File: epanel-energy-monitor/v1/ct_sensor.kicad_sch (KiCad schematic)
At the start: 8 parts

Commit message: add small terminal footprint
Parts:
- J?: footprint (none) -> mylife-footprints:RS PRO Terminal Small x2
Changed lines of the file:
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@@
       (effects (font (size 1.27 1.27)) (justify left))
     )
-    (property "Footprint" "" (id 2) (at 209.55 76.2 0)
+    (property "Footprint" "mylife-footprints:RS PRO Terminal Small x2" (id 2) (at 209.55 76.2 0)
       (effects (font (size 1.27 1.27)) hide)
     )
-    (property "Datasheet" "~" (id 3) (at 209.55 76.2 0)
+    (property "Datasheet" "https://docs.rs-online.com/90f4/0900766b8157c7e9.pdf" (id 3) (at 209.55 76.2 0)
       (effects (font (size 1.27 1.27)) hide)
     )

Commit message: rotary switch
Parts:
- removed J?: Conn_02x05, Connector_PinHeader_2.54mm:PinHeader_2x05_P2.54mm_Vertical, symbol Connector_Generic:Conn_02x05_Odd_Even
- added S15: SS-10-15SPE, mylife-footprints:RS PRO SS-10-15SPE, symbol mylife-symbols:SS-10-15SPE
- gave numbers to parts that had none: 7
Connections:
- net ZERO: now also S15.2 (Common), S15.7 (Common)
- net at R96.2: now also S15.3 (pos_2)
- net at R98.2: now also S15.5 (pos_4)
- net at R99.2: now also S15.6 (pos_5)
- net at R95.2: now also S15.1 (pos_1)
- net at R97.2: now also S15.4 (pos_3)

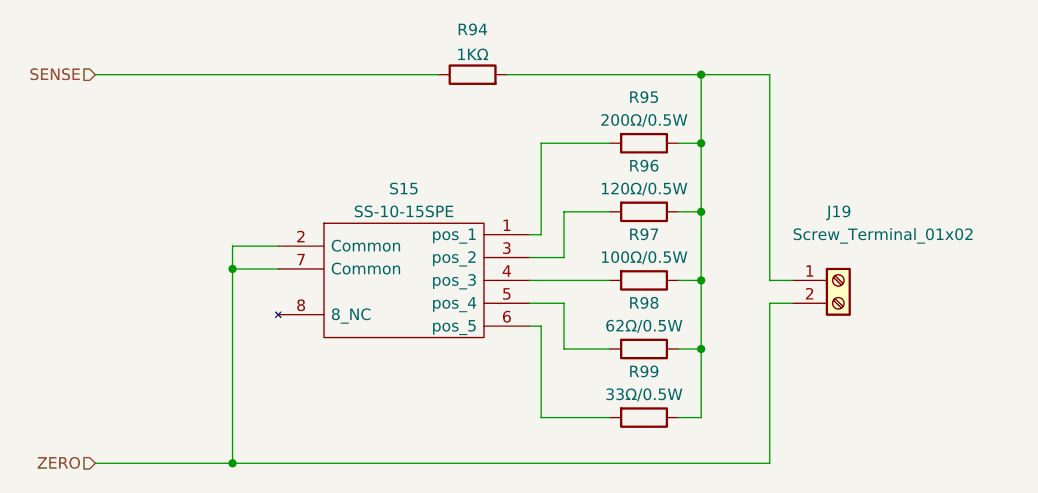
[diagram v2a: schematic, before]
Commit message: schematic remove esp
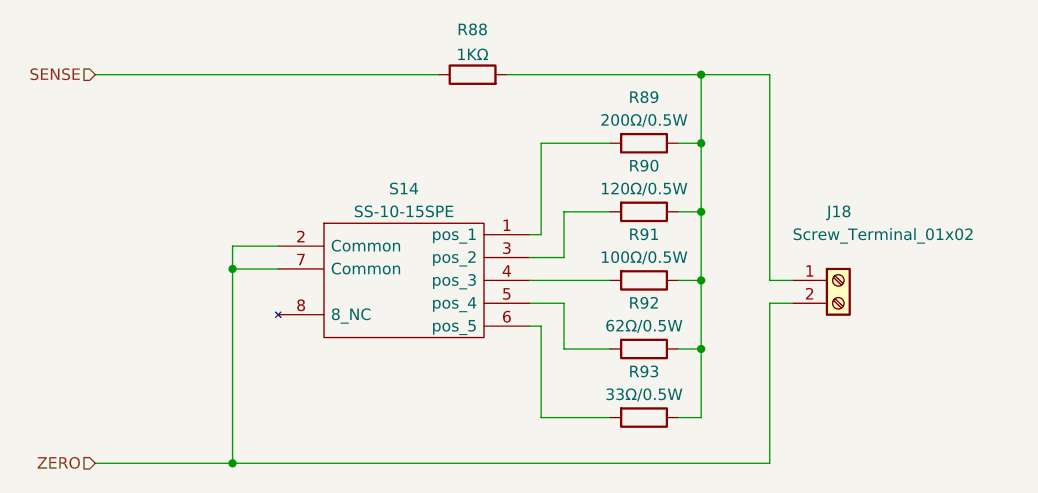
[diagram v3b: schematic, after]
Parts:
- renumbered J19 to J18, R94 to R88, R95 to R89, R96 to R90, R97 to R91, R98 to R92, R99 to R93, S15 to S14
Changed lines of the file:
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@@
   (symbol (lib_id "Device:R") (at 187.96 68.58 270)
     (in_bom yes) (on_board yes)
-    (property "Reference" "R96" (id 0) (at 187.96 63.5 90))
+    (property "Reference" "R90" (id 0) (at 187.96 63.5 90))
     (property "Value" "120Ω/0.5W" (id 1) (at 187.96 66.04 90))
     (property "Footprint" "Resistor_SMD:R_0805_2012Metric" (id 2) (at 187.96 66.802 90)
@@
   (symbol (lib_id "Device:R") (at 187.96 83.82 270)
     (in_bom yes) (on_board yes)
-    (property "Reference" "R98" (id 0) (at 187.96 78.74 90))
+    (property "Reference" "R92" (id 0) (at 187.96 78.74 90))
     (property "Value" "62Ω/0.5W" (id 1) (at 187.96 81.28 90))
     (property "Footprint" "Resistor_SMD:R_0805_2012Metric" (id 2) (at 187.96 82.042 90)
@@
   (symbol (lib_id "Device:R") (at 168.91 53.34 90)
     (in_bom yes) (on_board yes) (fields_autoplaced)
-    (property "Reference" "R94" (id 0) (at 168.91 48.3575 90))
+    (property "Reference" "R88" (id 0) (at 168.91 48.3575 90))
     (property "Value" "1KΩ" (id 1) (at 168.91 51.1326 90))
     (property "Footprint" "Resistor_SMD:R_0603_1608Metric" (id 2) (at 168.91 55.118 90)
@@
   (symbol (lib_id "Connector:Screw_Terminal_01x02") (at 209.55 76.2 0)
     (in_bom yes) (on_board yes)
-    (property "Reference" "J19" (id 0) (at 208.28 68.58 0)
+    (property "Reference" "J18" (id 0) (at 208.28 68.58 0)
       (effects (font (size 1.27 1.27)) (justify left))
     )
@@
   (symbol (lib_id "Device:R") (at 187.96 60.96 270)
     (in_bom yes) (on_board yes)
-    (property "Reference" "R95" (id 0) (at 187.96 55.88 90))
+    (property "Reference" "R89" (id 0) (at 187.96 55.88 90))
     (property "Value" "200Ω/0.5W" (id 1) (at 187.96 58.42 90))
     (property "Footprint" "Resistor_SMD:R_0805_2012Metric" (id 2) (at 187.96 59.182 90)
@@
   (symbol (lib_id "mylife-symbols:SS-10-15SPE") (at 161.29 76.2 0)
     (in_bom yes) (on_board yes)
-    (property "Reference" "S15" (id 0) (at 161.29 66.04 0))
+    (property "Reference" "S14" (id 0) (at 161.29 66.04 0))
     (property "Value" "SS-10-15SPE" (id 1) (at 161.29 68.58 0))
     (property "Footprint" "mylife-footprints:RS PRO SS-10-15SPE" (id 2) (at 185.42 73.66 0)
@@
   (symbol (lib_id "Device:R") (at 187.96 91.44 270)
     (in_bom yes) (on_board yes)
-    (property "Reference" "R99" (id 0) (at 187.96 86.36 90))
+    (property "Reference" "R93" (id 0) (at 187.96 86.36 90))
     (property "Value" "33Ω/0.5W" (id 1) (at 187.96 88.9 90))
     (property "Footprint" "Resistor_SMD:R_0805_2012Metric" (id 2) (at 187.96 89.662 90)
@@
   (symbol (lib_id "Device:R") (at 187.96 76.2 270)
     (in_bom yes) (on_board yes)
-    (property "Reference" "R97" (id 0) (at 187.96 71.12 90))
+    (property "Reference" "R91" (id 0) (at 187.96 71.12 90))
     (property "Value" "100Ω/0.5W" (id 1) (at 187.96 73.66 90))
     (property "Footprint" "Resistor_SMD:R_0805_2012Metric" (id 2) (at 187.96 74.422 90)

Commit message: enery monitor schematic
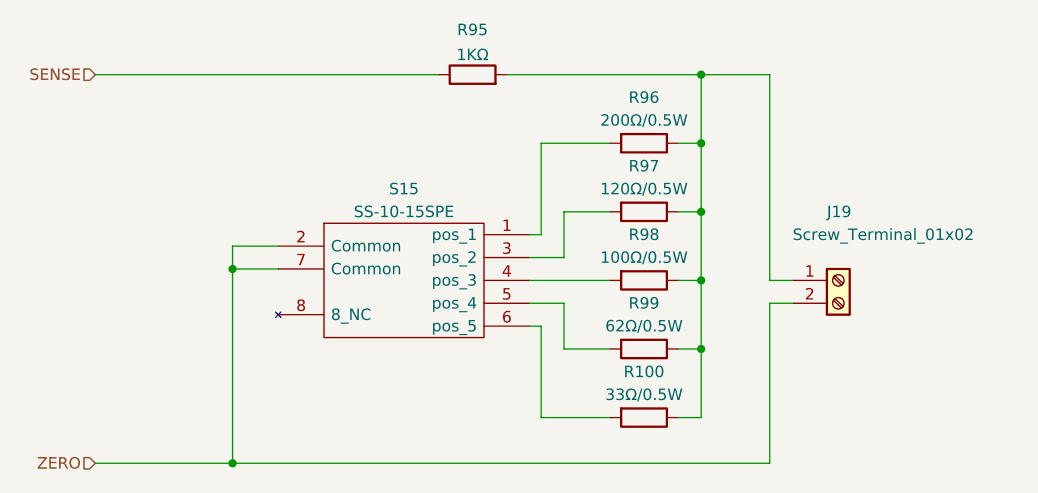
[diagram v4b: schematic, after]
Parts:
- renumbered J18 to J19, R93 to R100, R88 to R95, R89 to R96, R90 to R97, R91 to R98, R92 to R99, S14 to S15
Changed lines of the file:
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@@
   (symbol (lib_id "Device:R") (at 187.96 68.58 270)
     (in_bom yes) (on_board yes)
-    (property "Reference" "R90" (id 0) (at 187.96 63.5 90))
+    (property "Reference" "R97" (id 0) (at 187.96 63.5 90))
     (property "Value" "120Ω/0.5W" (id 1) (at 187.96 66.04 90))
     (property "Footprint" "Resistor_SMD:R_0805_2012Metric" (id 2) (at 187.96 66.802 90)
@@
   (symbol (lib_id "Device:R") (at 187.96 83.82 270)
     (in_bom yes) (on_board yes)
-    (property "Reference" "R92" (id 0) (at 187.96 78.74 90))
+    (property "Reference" "R99" (id 0) (at 187.96 78.74 90))
     (property "Value" "62Ω/0.5W" (id 1) (at 187.96 81.28 90))
     (property "Footprint" "Resistor_SMD:R_0805_2012Metric" (id 2) (at 187.96 82.042 90)
@@
   (symbol (lib_id "Device:R") (at 168.91 53.34 90)
     (in_bom yes) (on_board yes) (fields_autoplaced)
-    (property "Reference" "R88" (id 0) (at 168.91 48.3575 90))
+    (property "Reference" "R95" (id 0) (at 168.91 48.3575 90))
     (property "Value" "1KΩ" (id 1) (at 168.91 51.1326 90))
     (property "Footprint" "Resistor_SMD:R_0603_1608Metric" (id 2) (at 168.91 55.118 90)
@@
   (symbol (lib_id "Connector:Screw_Terminal_01x02") (at 209.55 76.2 0)
     (in_bom yes) (on_board yes)
-    (property "Reference" "J18" (id 0) (at 208.28 68.58 0)
+    (property "Reference" "J19" (id 0) (at 208.28 68.58 0)
       (effects (font (size 1.27 1.27)) (justify left))
     )
@@
   (symbol (lib_id "Device:R") (at 187.96 60.96 270)
     (in_bom yes) (on_board yes)
-    (property "Reference" "R89" (id 0) (at 187.96 55.88 90))
+    (property "Reference" "R96" (id 0) (at 187.96 55.88 90))
     (property "Value" "200Ω/0.5W" (id 1) (at 187.96 58.42 90))
     (property "Footprint" "Resistor_SMD:R_0805_2012Metric" (id 2) (at 187.96 59.182 90)
@@
   (symbol (lib_id "mylife-symbols:SS-10-15SPE") (at 161.29 76.2 0)
     (in_bom yes) (on_board yes)
-    (property "Reference" "S14" (id 0) (at 161.29 66.04 0))
+    (property "Reference" "S15" (id 0) (at 161.29 66.04 0))
     (property "Value" "SS-10-15SPE" (id 1) (at 161.29 68.58 0))
     (property "Footprint" "mylife-footprints:RS PRO SS-10-15SPE" (id 2) (at 185.42 73.66 0)
@@
   (symbol (lib_id "Device:R") (at 187.96 91.44 270)
     (in_bom yes) (on_board yes)
-    (property "Reference" "R93" (id 0) (at 187.96 86.36 90))
+    (property "Reference" "R100" (id 0) (at 187.96 86.36 90))
     (property "Value" "33Ω/0.5W" (id 1) (at 187.96 88.9 90))
     (property "Footprint" "Resistor_SMD:R_0805_2012Metric" (id 2) (at 187.96 89.662 90)
@@
   (symbol (lib_id "Device:R") (at 187.96 76.2 270)
     (in_bom yes) (on_board yes)
-    (property "Reference" "R91" (id 0) (at 187.96 71.12 90))
+    (property "Reference" "R98" (id 0) (at 187.96 71.12 90))
     (property "Value" "100Ω/0.5W" (id 1) (at 187.96 73.66 90))
     (property "Footprint" "Resistor_SMD:R_0805_2012Metric" (id 2) (at 187.96 74.422 90)

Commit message: wip energy pcb
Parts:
- renumbered J19 to J5, R95 to R11, R96 to R12, R97 to R13, R98 to R14, R99 to R15, R100 to R16, S15 to S1
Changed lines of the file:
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@@
   (symbol (lib_id "Device:R") (at 187.96 68.58 270)
     (in_bom yes) (on_board yes)
-    (property "Reference" "R97" (id 0) (at 187.96 63.5 90))
+    (property "Reference" "R13" (id 0) (at 187.96 63.5 90))
     (property "Value" "120Ω/0.5W" (id 1) (at 187.96 66.04 90))
     (property "Footprint" "Resistor_SMD:R_0805_2012Metric" (id 2) (at 187.96 66.802 90)
@@
   (symbol (lib_id "Device:R") (at 187.96 83.82 270)
     (in_bom yes) (on_board yes)
-    (property "Reference" "R99" (id 0) (at 187.96 78.74 90))
+    (property "Reference" "R15" (id 0) (at 187.96 78.74 90))
     (property "Value" "62Ω/0.5W" (id 1) (at 187.96 81.28 90))
     (property "Footprint" "Resistor_SMD:R_0805_2012Metric" (id 2) (at 187.96 82.042 90)
@@
   (symbol (lib_id "Device:R") (at 168.91 53.34 90)
     (in_bom yes) (on_board yes) (fields_autoplaced)
-    (property "Reference" "R95" (id 0) (at 168.91 48.3575 90))
+    (property "Reference" "R11" (id 0) (at 168.91 48.3575 90))
     (property "Value" "1KΩ" (id 1) (at 168.91 51.1326 90))
     (property "Footprint" "Resistor_SMD:R_0603_1608Metric" (id 2) (at 168.91 55.118 90)
@@
   (symbol (lib_id "Connector:Screw_Terminal_01x02") (at 209.55 76.2 0)
     (in_bom yes) (on_board yes)
-    (property "Reference" "J19" (id 0) (at 208.28 68.58 0)
+    (property "Reference" "J5" (id 0) (at 208.28 68.58 0)
       (effects (font (size 1.27 1.27)) (justify left))
     )
@@
   (symbol (lib_id "Device:R") (at 187.96 60.96 270)
     (in_bom yes) (on_board yes)
-    (property "Reference" "R96" (id 0) (at 187.96 55.88 90))
+    (property "Reference" "R12" (id 0) (at 187.96 55.88 90))
     (property "Value" "200Ω/0.5W" (id 1) (at 187.96 58.42 90))
     (property "Footprint" "Resistor_SMD:R_0805_2012Metric" (id 2) (at 187.96 59.182 90)
@@
   (symbol (lib_id "mylife-symbols:SS-10-15SPE") (at 161.29 76.2 0)
     (in_bom yes) (on_board yes)
-    (property "Reference" "S15" (id 0) (at 161.29 66.04 0))
+    (property "Reference" "S1" (id 0) (at 161.29 66.04 0))
     (property "Value" "SS-10-15SPE" (id 1) (at 161.29 68.58 0))
     (property "Footprint" "mylife-footprints:RS PRO SS-10-15SPE" (id 2) (at 185.42 73.66 0)
@@
   (symbol (lib_id "Device:R") (at 187.96 91.44 270)
     (in_bom yes) (on_board yes)
-    (property "Reference" "R100" (id 0) (at 187.96 86.36 90))
+    (property "Reference" "R16" (id 0) (at 187.96 86.36 90))
     (property "Value" "33Ω/0.5W" (id 1) (at 187.96 88.9 90))
     (property "Footprint" "Resistor_SMD:R_0805_2012Metric" (id 2) (at 187.96 89.662 90)
@@
   (symbol (lib_id "Device:R") (at 187.96 76.2 270)
     (in_bom yes) (on_board yes)
-    (property "Reference" "R98" (id 0) (at 187.96 71.12 90))
+    (property "Reference" "R14" (id 0) (at 187.96 71.12 90))
     (property "Value" "100Ω/0.5W" (id 1) (at 187.96 73.66 90))
     (property "Footprint" "Resistor_SMD:R_0805_2012Metric" (id 2) (at 187.96 74.422 90)

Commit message: wip energy pcb
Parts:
- renumbered J5 to J18, R11 to R89, R12 to R90, R13 to R91, R14 to R92, R15 to R93, R16 to R94, S1 to S14
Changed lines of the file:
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@@
   (symbol (lib_id "Device:R") (at 187.96 68.58 270)
     (in_bom yes) (on_board yes)
-    (property "Reference" "R13" (id 0) (at 187.96 63.5 90))
+    (property "Reference" "R91" (id 0) (at 187.96 63.5 90))
     (property "Value" "120Ω/0.5W" (id 1) (at 187.96 66.04 90))
     (property "Footprint" "Resistor_SMD:R_0805_2012Metric" (id 2) (at 187.96 66.802 90)
@@
   (symbol (lib_id "Device:R") (at 187.96 83.82 270)
     (in_bom yes) (on_board yes)
-    (property "Reference" "R15" (id 0) (at 187.96 78.74 90))
+    (property "Reference" "R93" (id 0) (at 187.96 78.74 90))
     (property "Value" "62Ω/0.5W" (id 1) (at 187.96 81.28 90))
     (property "Footprint" "Resistor_SMD:R_0805_2012Metric" (id 2) (at 187.96 82.042 90)
@@
   (symbol (lib_id "Device:R") (at 168.91 53.34 90)
     (in_bom yes) (on_board yes) (fields_autoplaced)
-    (property "Reference" "R11" (id 0) (at 168.91 48.3575 90))
+    (property "Reference" "R89" (id 0) (at 168.91 48.3575 90))
     (property "Value" "1KΩ" (id 1) (at 168.91 51.1326 90))
     (property "Footprint" "Resistor_SMD:R_0603_1608Metric" (id 2) (at 168.91 55.118 90)
@@
   (symbol (lib_id "Connector:Screw_Terminal_01x02") (at 209.55 76.2 0)
     (in_bom yes) (on_board yes)
-    (property "Reference" "J5" (id 0) (at 208.28 68.58 0)
+    (property "Reference" "J18" (id 0) (at 208.28 68.58 0)
       (effects (font (size 1.27 1.27)) (justify left))
     )
@@
   (symbol (lib_id "Device:R") (at 187.96 60.96 270)
     (in_bom yes) (on_board yes)
-    (property "Reference" "R12" (id 0) (at 187.96 55.88 90))
+    (property "Reference" "R90" (id 0) (at 187.96 55.88 90))
     (property "Value" "200Ω/0.5W" (id 1) (at 187.96 58.42 90))
     (property "Footprint" "Resistor_SMD:R_0805_2012Metric" (id 2) (at 187.96 59.182 90)
@@
   (symbol (lib_id "mylife-symbols:SS-10-15SPE") (at 161.29 76.2 0)
     (in_bom yes) (on_board yes)
-    (property "Reference" "S1" (id 0) (at 161.29 66.04 0))
+    (property "Reference" "S14" (id 0) (at 161.29 66.04 0))
     (property "Value" "SS-10-15SPE" (id 1) (at 161.29 68.58 0))
     (property "Footprint" "mylife-footprints:RS PRO SS-10-15SPE" (id 2) (at 185.42 73.66 0)
@@
   (symbol (lib_id "Device:R") (at 187.96 91.44 270)
     (in_bom yes) (on_board yes)
-    (property "Reference" "R16" (id 0) (at 187.96 86.36 90))
+    (property "Reference" "R94" (id 0) (at 187.96 86.36 90))
     (property "Value" "33Ω/0.5W" (id 1) (at 187.96 88.9 90))
     (property "Footprint" "Resistor_SMD:R_0805_2012Metric" (id 2) (at 187.96 89.662 90)
@@
   (symbol (lib_id "Device:R") (at 187.96 76.2 270)
     (in_bom yes) (on_board yes)
-    (property "Reference" "R14" (id 0) (at 187.96 71.12 90))
+    (property "Reference" "R92" (id 0) (at 187.96 71.12 90))
     (property "Value" "100Ω/0.5W" (id 1) (at 187.96 73.66 90))
     (property "Footprint" "Resistor_SMD:R_0805_2012Metric" (id 2) (at 187.96 74.422 90)

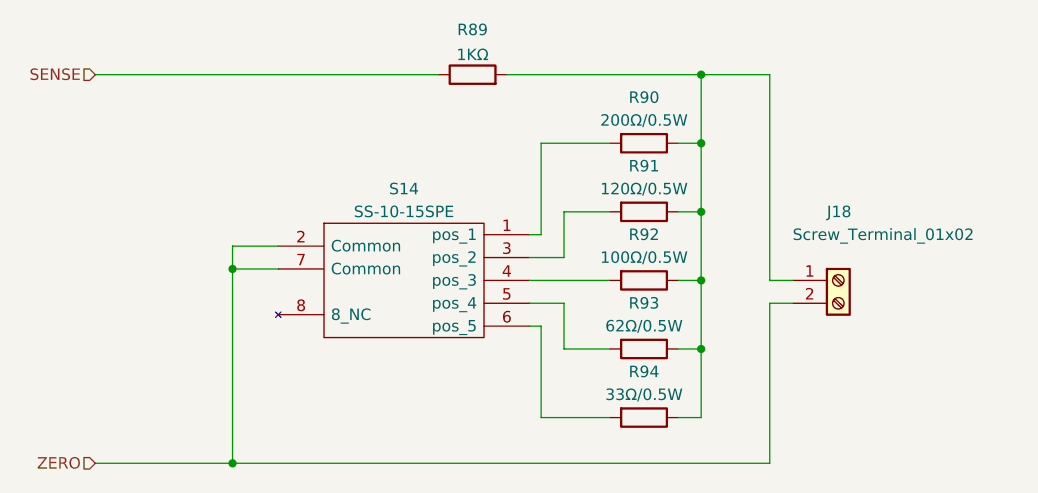
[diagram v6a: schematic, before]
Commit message: fix annotations
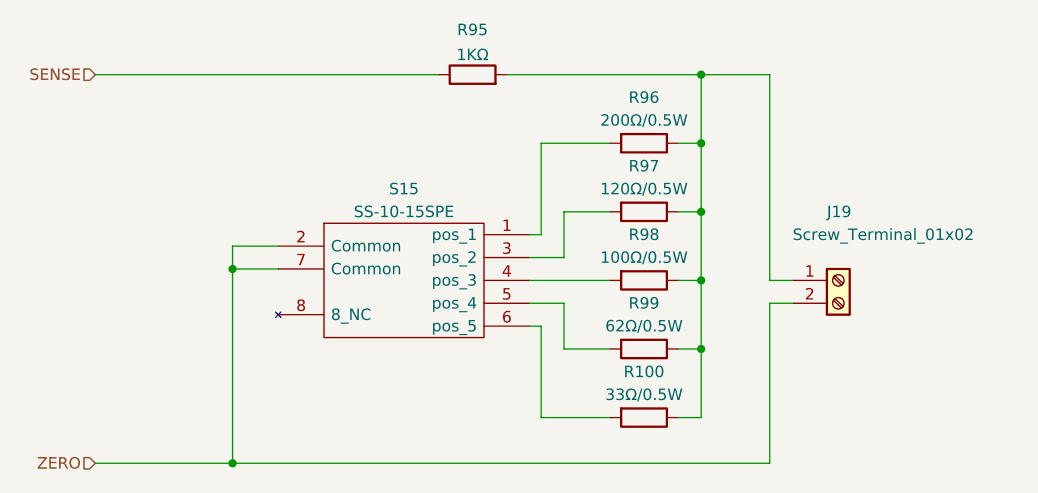
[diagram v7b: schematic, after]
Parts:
- renumbered J18 to J19, R94 to R100, R89 to R95, R90 to R96, R91 to R97, R92 to R98, R93 to R99, S14 to S15
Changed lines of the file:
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@@
   (symbol (lib_id "Device:R") (at 187.96 68.58 270)
     (in_bom yes) (on_board yes)
-    (property "Reference" "R91" (id 0) (at 187.96 63.5 90))
+    (property "Reference" "R97" (id 0) (at 187.96 63.5 90))
     (property "Value" "120Ω/0.5W" (id 1) (at 187.96 66.04 90))
     (property "Footprint" "Resistor_SMD:R_0805_2012Metric" (id 2) (at 187.96 66.802 90)
@@
   (symbol (lib_id "Device:R") (at 187.96 83.82 270)
     (in_bom yes) (on_board yes)
-    (property "Reference" "R93" (id 0) (at 187.96 78.74 90))
+    (property "Reference" "R99" (id 0) (at 187.96 78.74 90))
     (property "Value" "62Ω/0.5W" (id 1) (at 187.96 81.28 90))
     (property "Footprint" "Resistor_SMD:R_0805_2012Metric" (id 2) (at 187.96 82.042 90)
@@
   (symbol (lib_id "Device:R") (at 168.91 53.34 90)
     (in_bom yes) (on_board yes) (fields_autoplaced)
-    (property "Reference" "R89" (id 0) (at 168.91 48.3575 90))
+    (property "Reference" "R95" (id 0) (at 168.91 48.3575 90))
     (property "Value" "1KΩ" (id 1) (at 168.91 51.1326 90))
     (property "Footprint" "Resistor_SMD:R_0603_1608Metric" (id 2) (at 168.91 55.118 90)
@@
   (symbol (lib_id "Connector:Screw_Terminal_01x02") (at 209.55 76.2 0)
     (in_bom yes) (on_board yes)
-    (property "Reference" "J18" (id 0) (at 208.28 68.58 0)
+    (property "Reference" "J19" (id 0) (at 208.28 68.58 0)
       (effects (font (size 1.27 1.27)) (justify left))
     )
@@
   (symbol (lib_id "Device:R") (at 187.96 60.96 270)
     (in_bom yes) (on_board yes)
-    (property "Reference" "R90" (id 0) (at 187.96 55.88 90))
+    (property "Reference" "R96" (id 0) (at 187.96 55.88 90))
     (property "Value" "200Ω/0.5W" (id 1) (at 187.96 58.42 90))
     (property "Footprint" "Resistor_SMD:R_0805_2012Metric" (id 2) (at 187.96 59.182 90)
@@
   (symbol (lib_id "mylife-symbols:SS-10-15SPE") (at 161.29 76.2 0)
     (in_bom yes) (on_board yes)
-    (property "Reference" "S14" (id 0) (at 161.29 66.04 0))
+    (property "Reference" "S15" (id 0) (at 161.29 66.04 0))
     (property "Value" "SS-10-15SPE" (id 1) (at 161.29 68.58 0))
     (property "Footprint" "mylife-footprints:RS PRO SS-10-15SPE" (id 2) (at 185.42 73.66 0)
@@
   (symbol (lib_id "Device:R") (at 187.96 91.44 270)
     (in_bom yes) (on_board yes)
-    (property "Reference" "R94" (id 0) (at 187.96 86.36 90))
+    (property "Reference" "R100" (id 0) (at 187.96 86.36 90))
     (property "Value" "33Ω/0.5W" (id 1) (at 187.96 88.9 90))
     (property "Footprint" "Resistor_SMD:R_0805_2012Metric" (id 2) (at 187.96 89.662 90)
@@
   (symbol (lib_id "Device:R") (at 187.96 76.2 270)
     (in_bom yes) (on_board yes)
-    (property "Reference" "R92" (id 0) (at 187.96 71.12 90))
+    (property "Reference" "R98" (id 0) (at 187.96 71.12 90))
     (property "Value" "100Ω/0.5W" (id 1) (at 187.96 73.66 90))
     (property "Footprint" "Resistor_SMD:R_0805_2012Metric" (id 2) (at 187.96 74.422 90)
